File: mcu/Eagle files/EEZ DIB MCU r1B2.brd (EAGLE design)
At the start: 139 x 70 mm, 194 parts, among them IC1 TPD4E001DRLR, IC10 TPS2051BDBVR, IC11 TPS61169DCKR, IC12 TPD4E001DRLR, IC13 TPA6205A1DGN, IC14 TPD4E001DRLR, IC15 AR1021-I/SS, IC16 TPD4E001DRLR, IC17 DP83848CVV/NOPB, IC2 SN74LVC2G34DBVR, IC3 BTS3408G, IC4 STM32F769IGT6, IC5 LD1117ADT33TR, IC6 TPD4E001DRLR, IC7 TPD4E001DRLR, IC8 IS42S16400J, IC9 BR24G64FVT-3AGE2, J1 503398-1892, J2 67803-8020, Q1 MMBT5551, SW1 PEC16-2215F-S0024, SW2 TL1100CF160Q, X1 ZL263-40DG, X2 ZL231-16KG, X3 1844249, X4 ZL231-20KG, X5 LMJTAB881243M-L, Y1 10MHz

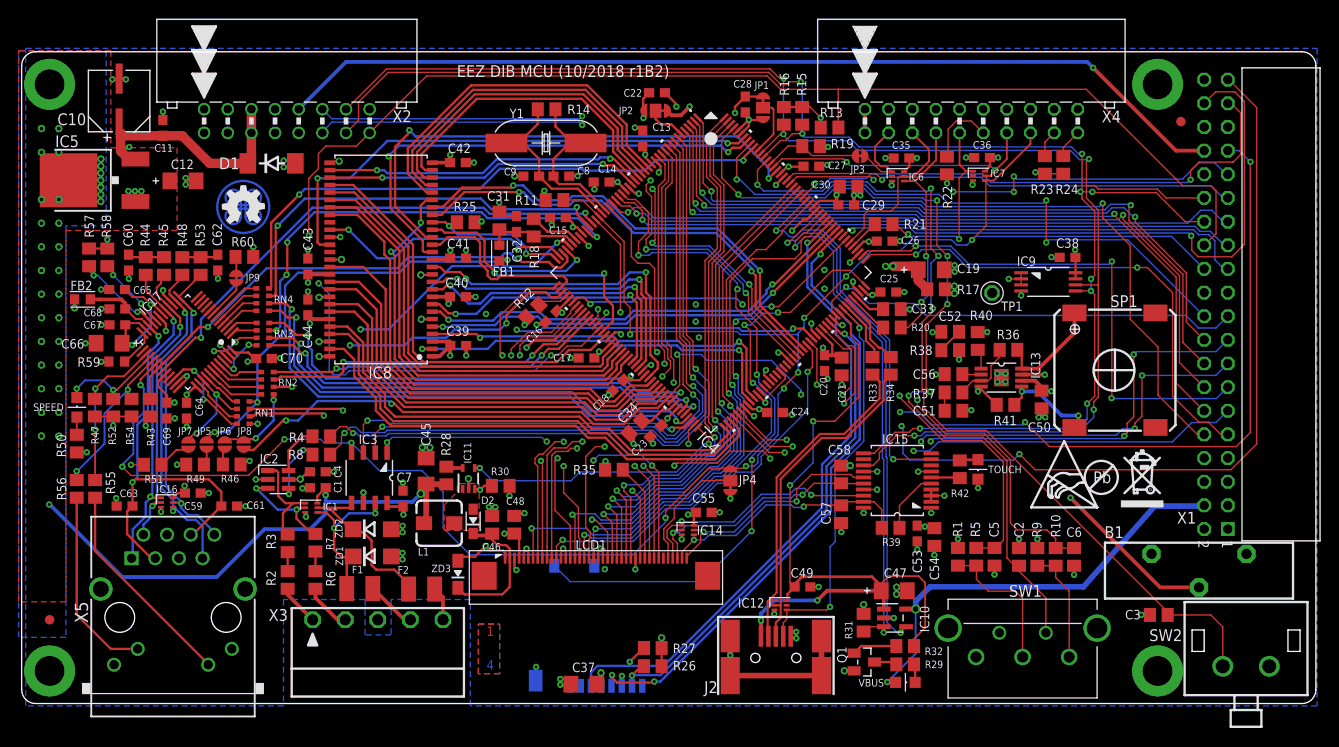
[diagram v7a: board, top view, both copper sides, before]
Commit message: MCU fixes: #10, #13, #15, #16, #17, #18
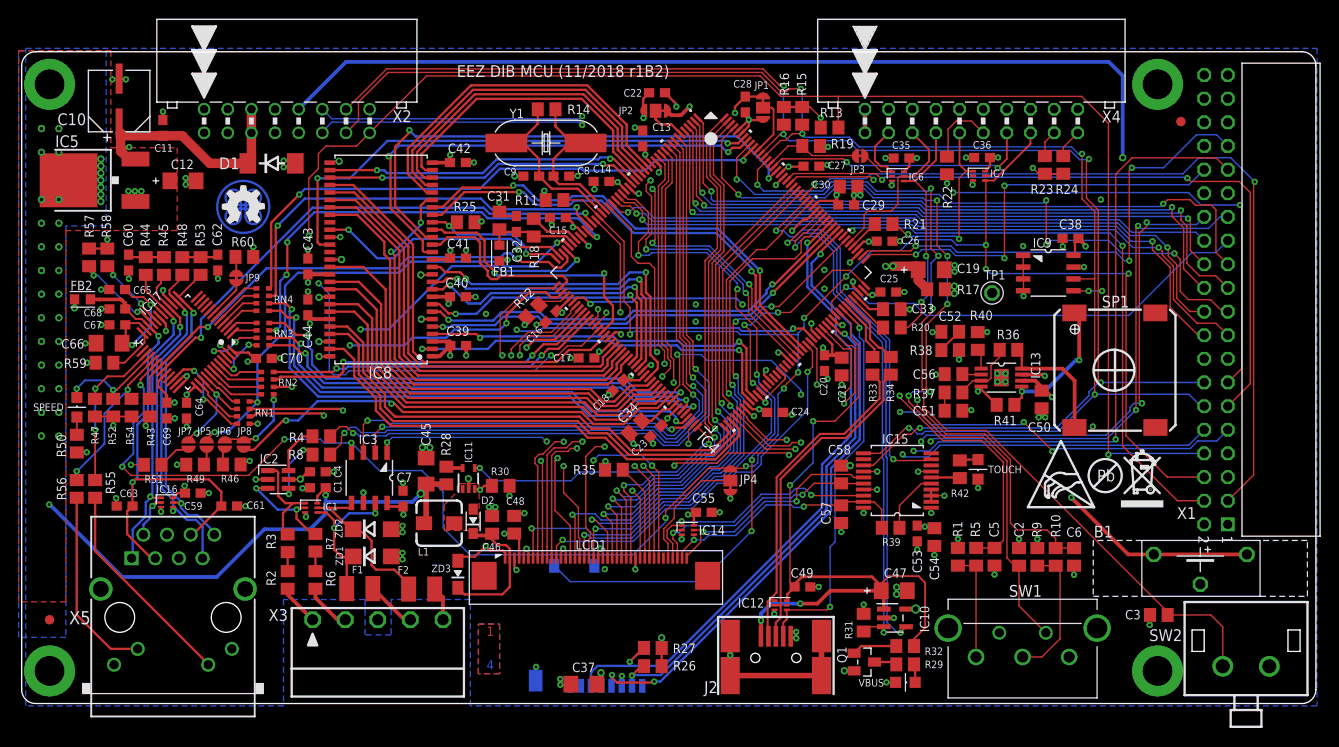
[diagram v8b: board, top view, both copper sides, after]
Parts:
- B1: value DS1092-16-B6P -> S8401-46 or DS1092-16-B6P; device EEZ_Lib1:DS1092-16-B6P -> EEZ_Lib1:S8401-46
- IC9: value BR24G64FVT-3AGE2 -> AT24C02D-SSHM-T; device EEZ_DIB:PW8_TSSOP8 -> EEZ_Lib1:SOIC127P600X173-8N
- R29: value 47K -> 220R
- R59: device rcl:R0603 -> rcl:R0805
- Y1: value 10MHz -> 25MHz
- moved C38 2.06 mm to (108.1, 49.9)
- moved B1 1.75 mm to (122.1, 16.0), turned to 180 degrees
- moved R59 1.33 mm to (4.39, 36.6)
- moved IC9 0.95 mm to (105.8, 46.2)
- moved X1 0.50 mm to (122.5, 67.5)
- moved U$5 0.46 mm to (111.9, 24.5)
- moved U$6 0.34 mm to (103.6, 21.1)
- moved C14 0.06 mm to (57.8, 56.1)
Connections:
- net !FAULT: now also X1.8; no longer X1.26
- net !RESET: now also X1.6; no longer X1.24
- net +12V: now also X1.37, X1.38; no longer X1.5, X1.6
- net +3V3: now also VBUS.A, X1.7; no longer IC9.1, IC9.2, IC9.3, IC9.7, X1.32
- net +5V: now also X1.35, X1.36; no longer VBUS.A, X1.3, X1.4
- net +VAUX: now also X1.5; no longer X1.34
- net EOUT_A: now also SW1.B; no longer SW1.A
- net EOUT_B: now also SW1.A; no longer SW1.B
- net GND: now also B1.2, IC9.1, IC9.2, IC9.3, IC9.7, X1.15, X1.16, X1.29, X1.30, X1.34, X1.39; no longer B1.1, B1.3, X1.21, X1.22, X1.35, X1.36, X1.7, X1.8
- net I2C1_SCL: now also IC9.6, X1.12; no longer IC9.5, X1.28
- net I2C1_SDA: now also IC9.5, X1.14; no longer IC9.6, X1.30
- net N$166: now also SP1.-; no longer SP1.+
- net N$20: now also B1.1, B1.3; no longer B1.2
- net N$50: now also SP1.+; no longer SP1.-
- net OE_SYNC: now also X1.10; no longer X1.39
- net OUT_PAR: now also X1.4; no longer X1.38
- net OUT_SER: now also X1.3; no longer X1.37
- net SPI2_CLK: now also X1.32; no longer X1.9
- net SPI2_CSA: now also X1.28; no longer X1.15
- net SPI2_CSB: now also X1.27; no longer X1.17
- net SPI2_IRQ: now also X1.25; no longer X1.19
- net SPI2_MISO: now also X1.31; no longer X1.11
- net SPI2_MOSI: now also X1.33; no longer X1.13
- net SPI4_CLK: now also X1.23; no longer X1.10
- net SPI4_CSA: now also X1.22; no longer X1.16
- net SPI4_CSB: now also X1.21; no longer X1.18
- net SPI4_IRQ: now also X1.19; no longer X1.20
- net SPI4_MISO: now also X1.24; no longer X1.12
- net SPI4_MOSI: now also X1.26; no longer X1.14
- net SPI5_CLK: now also X1.17; no longer X1.23
- net SPI5_CSA: now also X1.11; no longer X1.29
- net SPI5_CSB: now also X1.13; no longer X1.31
- net SPI5_IRQ: now also X1.9; no longer X1.33
- net SPI5_MISO: now also X1.18; no longer X1.25
- net SPI5_MOSI: now also X1.20; no longer X1.27
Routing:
- net OE_SYNC: track 103.2 -> 55.6 mm, vias 3 -> 2
- net +VAUX: track 103.3 -> 147.7 mm
- net +5V: track 182.3 -> 223.9 mm, vias 7 -> 6
- net SPI5_IRQ: track 154.0 -> 120.2 mm
- net OUT_SER: track 56.6 -> 86.9 mm
- net SPI2_MISO: track 68.1 -> 96.1 mm, vias 4 -> 5
- net SPI5_CSA: track 49.0 -> 75.1 mm, vias 1 -> 2
- net !FAULT: track 199.4 -> 223.5 mm, vias 5 -> 6
- net !RESET: track 214.1 -> 234.6 mm, vias 12 -> 14
- net SPI5_CSB: track 51.6 -> 70.2 mm, vias 4 -> 3
- net SPI4_MOSI: track 78.0 -> 65.3 mm, vias 2 -> 1
- net SPI2_CSA: track 61.0 -> 73.5 mm
- net SPI2_CSB: track 64.4 -> 76.7 mm
- net SPI4_MISO: track 79.5 -> 67.9 mm
- net SPI4_CLK: track 81.6 -> 71.0 mm
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- added copper zone on layer 2, net +12V
- removed copper zone on layer 15, net +12V
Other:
- board text added: "EEZ DIB MCU (11/2018 r1B2)"
- board text removed: "EEZ DIB MCU (10/2018 r1B2)"
